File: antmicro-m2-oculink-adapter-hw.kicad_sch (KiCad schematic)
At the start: 10 parts, among them J1 PCB-Edge_M.2_Key-M, J2 OCuLink_x4_Amphenol_G14A42121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

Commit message: [#80280] Fix DRC
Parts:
- added TP3: TP_1.5mm_SMD, antmicro-footprints:TP_SMD_1.5mm, symbol TestPoints:TP_1.5mm_SMD
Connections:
- net at J2.B13 (~{CPRSNT}): now also TP3.1
- no-connect marks 8 -> 7
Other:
- moved on the sheet: R5
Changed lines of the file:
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@@
 		(title " M.2 to OCuLink adapter")
 		(date "2025-07-09")
-		(rev "0")
+		(rev "1.0.0")
 		(company "Antmicro Ltd")
 		(comment 1 "www.antmicro.com")
@@
 	)
 	(no_connect
-		(at 250.19 80.01)
-	)
-	(no_connect
 		(at 55.88 82.55)
 	)
@@
 	(wire
 		(pts
-			(xy 229.87 82.55) (xy 224.79 82.55)
+			(xy 232.41 82.55) (xy 227.33 82.55)
 		)
 		(stroke
@@
 	(wire
 		(pts
-			(xy 250.19 82.55) (xy 234.95 82.55)
+			(xy 250.19 82.55) (xy 237.49 82.55)
 		)
 		(stroke
@@
 	(wire
 		(pts
-			(xy 229.87 77.47) (xy 224.79 77.47)
+			(xy 232.41 77.47) (xy 227.33 77.47)
 		)
 		(stroke
@@
 	(wire
 		(pts
-			(xy 250.19 77.47) (xy 234.95 77.47)
+			(xy 250.19 77.47) (xy 237.49 77.47)
 		)
 		(stroke
@@
 		(pts
 			(xy 40.64 86.36) (xy 40.64 87.63)
+		)
+		(stroke
+			(width 0)
+			(type default)
+		)
+	)
+	(wire
+		(pts
+			(xy 214.63 80.01) (xy 250.19 80.01)
 		)
 		(stroke
@@
 	)
 	(label "~{WAKE}"
-		(at 224.79 82.55 180)
+		(at 227.33 82.55 180)
 		(effects
 			(font
@@
 	)
 	(label "~{PERST}"
-		(at 224.79 77.47 180)
+		(at 227.33 77.47 180)
 		(effects
 			(font
@@
 	)
 	(symbol
+		(lib_id "TestPoints:TP_1.5mm_SMD")
+		(at 214.63 80.01 90)
+		(unit 1)
+		(exclude_from_sim no)
+		(in_bom no)
+		(on_board yes)
+		(dnp no)
+		(property "Reference" "TP3"
+			(at 215.392 76.708 90)
+			(effects
+				(font
+					(size 1.27 1.27)
+					(thickness 0.15)
+				)
+				(justify right)
+			)
+		)
+		(property "Value" "TP_1.5mm_SMD"
+			(at 222.25 64.77 0)
+			(effects
+				(font
+					(size 1.27 1.27)
+					(thickness 0.15)
+				)
+				(justify left bottom)
+				(hide yes)
+			)
+		)
+		(property "Footprint" "antmicro-footprints:TP_SMD_1.5mm"
+			(at 224.79 64.77 0)
+			(effects
+				(font
+					(size 1.27 1.27)
+					(thickness 0.15)
+				)
+				(justify left bottom)
+				(hide yes)
+			)
+		)
+		(property "Datasheet" ""
+			(at 227.33 62.23 0)
+			(effects
+				(font
+					(size 1.27 1.27)
+					(thickness 0.15)
+				)
+				(justify left bottom)
+				(hide yes)
+			)
+		)
+		(property "Description" "test point, SMT"
+			(at 214.63 80.01 0)
+			(effects
+				(font
+					(size 1.27 1.27)
+				)
+				(hide yes)
+			)
+		)
+		(property "MPN" ""
+			(at 214.63 80.01 0)
+			(effects
+				(font
+					(size 1.27 1.27)
+				)
+				(hide yes)
+			)
+		)
+		(property "Manufacturer" ""
+			(at 214.63 80.01 0)
+			(effects
+				(font
+					(size 1.27 1.27)
+				)
+				(hide yes)
+			)
+		)
+		(property "Author" "Antmicro"
+			(at 229.87 64.77 0)
+			(effects
+				(font
+					(size 1.27 1.27)
+					(thickness 0.15)
+				)
+				(justify left bottom)
+				(hide yes)
+			)
+		)
+		(property "License" "Apache-2.0"
+			(at 232.41 64.77 0)
+			(effects
+				(font
+					(size 1.27 1.27)
+					(thickness 0.15)
+				)
+				(justify left bottom)
+				(hide yes)
+			)
+		)
+		(pin "1"
+		)
+		(instances
+			(project "antmicro-m2-oculink-adapter-hw"
+				(path "/b9cca87b-aef2-493b-be4f-d9e02584eafa"
+					(reference "TP3")
+					(unit 1)
+				)
+			)
+		)
+	)
+	(symbol
 		(lib_id "antmicropower:GND")
 		(at 278.13 146.05 0)
@@
 	(symbol
 		(lib_id "antmicroResistors0402:R_0R_0402")
-		(at 234.95 77.47 0)
+		(at 237.49 77.47 0)
 		(mirror y)
 		(unit 1)
@@
 		(dnp no)
 		(property "Reference" "R5"
-			(at 236.728 76.2 0)
+			(at 239.268 76.2 0)
 			(effects
 				(font
@@
 		)
 		(property "Value" "R_0R_0402"
-			(at 214.63 90.17 0)
+			(at 217.17 90.17 0)
 			(effects
 				(font
@@
 		)
 		(property "Footprint" "antmicro-footprints:R_0402_1005Metric"
-			(at 214.63 92.71 0)
+			(at 217.17 92.71 0)
 			(effects
 				(font
@@
 		)
 		(property "Datasheet" "https://industrial.panasonic.com/cdbs/www-data/pdf/RDA0000/AOA0000C301.pdf"
-			(at 214.63 95.25 0)
+			(at 217.17 95.25 0)
 			(effects
 				(font
@@
 		)
 		(property "Description" "SMD Chip Resistor, Jumper, 0 ohm, 100 mW, 0402 [1005 Metric], Thick Film, General Purpose"
-			(at 234.95 77.47 0)
+			(at 237.49 77.47 0)
 			(effects
 				(font
@@
 		)
 		(property "MPN" "ERJ2GE0R00X"
-			(at 214.63 97.79 0)
+			(at 217.17 97.79 0)
 			(effects
 				(font
@@
 		)
 		(property "Manufacturer" "Panasonic"
-			(at 214.63 100.33 0)
+			(at 217.17 100.33 0)
 			(effects
 				(font
@@
 		)
 		(property "License" "Apache-2.0"
-			(at 214.63 102.87 0)
+			(at 217.17 102.87 0)
 			(effects
 				(font
@@
 		)
 		(property "Author" "Antmicro"
-			(at 214.63 105.41 0)
+			(at 217.17 105.41 0)
 			(effects
 				(font
@@
 		)
 		(property "Val" "0R"
-			(at 228.854 76.2 0)
+			(at 231.394 76.2 0)
 			(effects
 				(font
@@
 		)
 		(property "Tolerance" "~"
-			(at 214.63 87.63 0)
+			(at 217.17 87.63 0)
 			(effects
 				(font
@@
 		)
 		(property "Current" "1A"
-			(at 214.63 107.95 0)
+			(at 217.17 107.95 0)
 			(effects
 				(font
@@
 	(symbol
 		(lib_id "antmicroResistors0402:R_0R_0402")
-		(at 234.95 82.55 0)
+		(at 237.49 82.55 0)
 		(mirror y)
 		(unit 1)
@@
 		(dnp no)
 		(property "Reference" "R6"
-			(at 236.728 81.28 0)
-			(effects
-				(font
-					(size 1.27 1.27)
-					(thickness 0.15)
-				)
-				(hide yes)
+			(at 239.268 81.28 0)
+			(effects
+				(font
+					(size 1.27 1.27)
+					(thickness 0.15)
+				)
 			)
 		)
 		(property "Value" "R_0R_0402"
-			(at 214.63 95.25 0)
+			(at 217.17 95.25 0)
 			(effects
 				(font
@@
 		)
 		(property "Footprint" "antmicro-footprints:R_0402_1005Metric"
-			(at 214.63 97.79 0)
+			(at 217.17 97.79 0)
 			(effects
 				(font
@@
 		)
 		(property "Datasheet" "https://industrial.panasonic.com/cdbs/www-data/pdf/RDA0000/AOA0000C301.pdf"
-			(at 214.63 100.33 0)
+			(at 217.17 100.33 0)
 			(effects
 				(font
@@
 		)
 		(property "Description" "SMD Chip Resistor, Jumper, 0 ohm, 100 mW, 0402 [1005 Metric], Thick Film, General Purpose"
-			(at 234.95 82.55 0)
+			(at 237.49 82.55 0)
 			(effects
 				(font
@@
 		)
 		(property "MPN" "ERJ2GE0R00X"
-			(at 214.63 102.87 0)
+			(at 217.17 102.87 0)
 			(effects
 				(font
@@
 		)
 		(property "Manufacturer" "Panasonic"
-			(at 214.63 105.41 0)
+			(at 217.17 105.41 0)
 			(effects
 				(font
@@
 		)
 		(property "License" "Apache-2.0"
-			(at 214.63 107.95 0)
+			(at 217.17 107.95 0)
 			(effects
 				(font
@@
 		)
 		(property "Author" "Antmicro"
-			(at 214.63 110.49 0)
+			(at 217.17 110.49 0)
 			(effects
 				(font
@@
 		)
 		(property "Val" "0R"
-			(at 228.854 81.28 0)
+			(at 231.394 81.28 0)
 			(effects
 				(font
@@
 		)
 		(property "Tolerance" "~"
-			(at 214.63 92.71 0)
+			(at 217.17 92.71 0)
 			(effects
 				(font
@@
 		)
 		(property "Current" "1A"
-			(at 214.63 113.03 0)
-			(effects
-				(font
+			(at 217.17 113.03 0)
+			(effects
+				(font

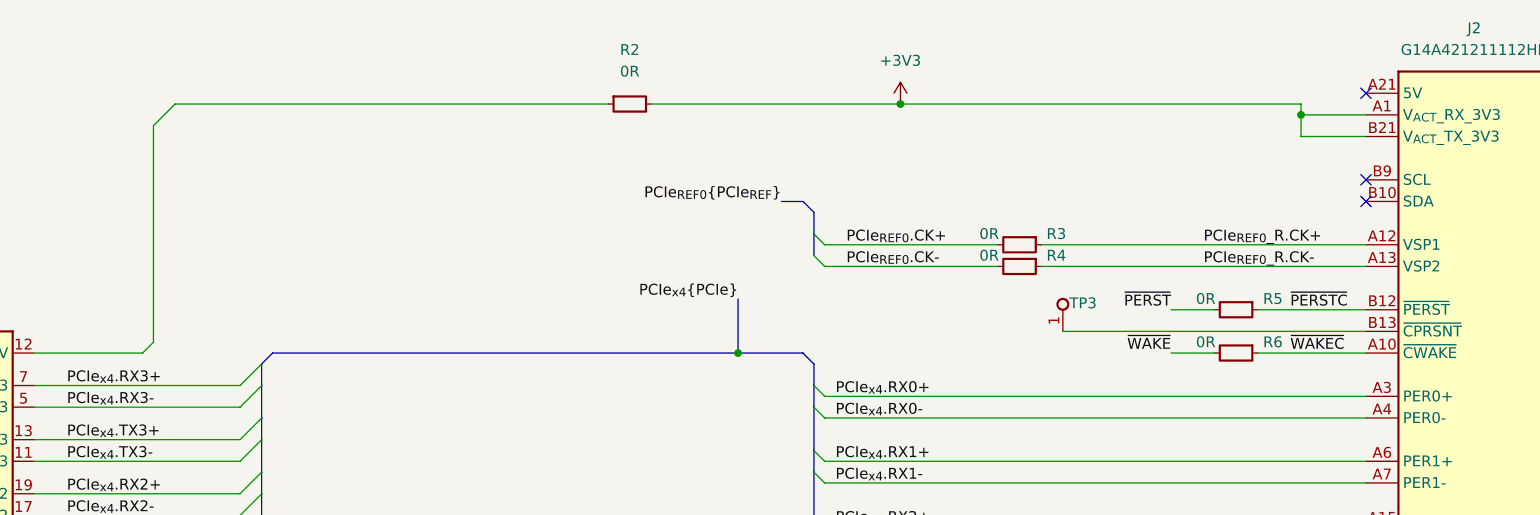
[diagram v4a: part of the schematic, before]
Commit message: [#81131] Change resistor, testpoint sizing. Add 0R to 3V3 and ~CWAKE
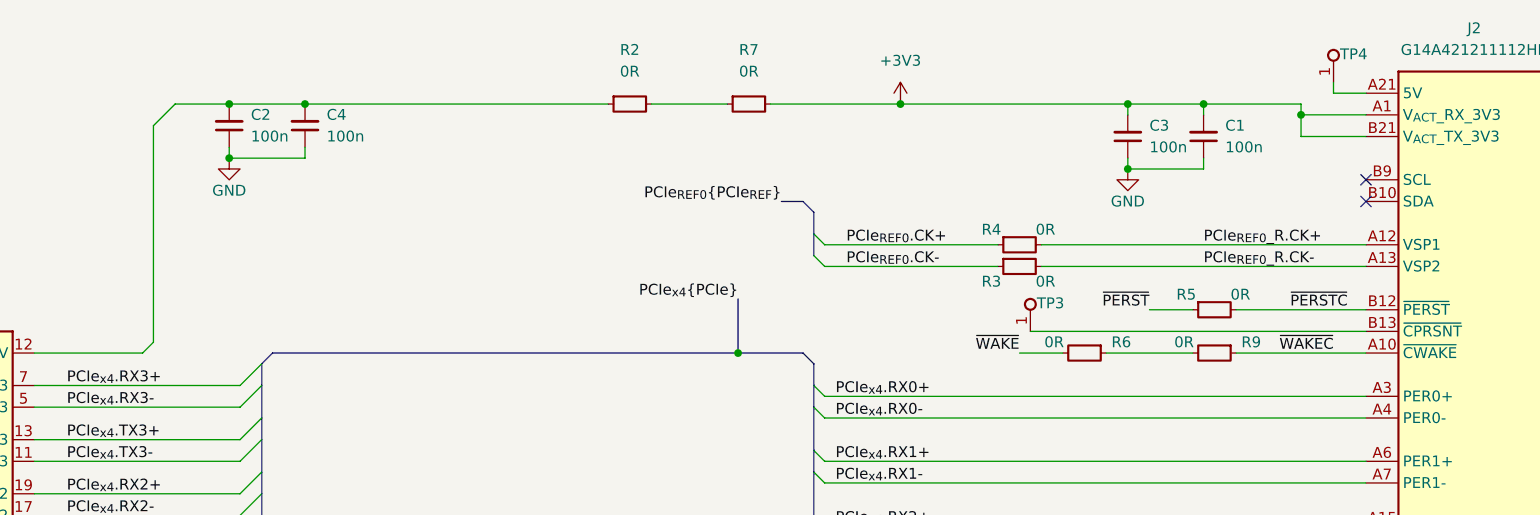
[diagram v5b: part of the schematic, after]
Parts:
- removed R3, R4, R5: R_0R_0402, antmicro-footprints:R_0402_1005Metric, symbol antmicroResistors0402:R_0R_0402
- added C1, C2, C3, C4: C_100n_16V_X7R_0402, antmicro-footprints:C_0402_1005Metric, symbol Capacitors0402:C_100n_16V_X7R_0402
- added R3, R4, R5: R_0R_0201, antmicro-footprints:R_0201, symbol antmicroResistorsmisc:R_0R_0201
- added R7: R_0R_0402, antmicro-footprints:R_0402_1005Metric, symbol Resistors0402:R_0R_0402
- added R9: R_0R_0402, antmicro-footprints:R_0402_1005Metric, symbol antmicroResistors0402:R_0R_0402
- added TP4: TP_1.5mm_SMD, antmicro-footprints:TP_SMD_1.5mm, symbol TestPoints:TP_1.5mm_SMD
- TP3: footprint antmicro-footprints:TP_SMD_1.5mm -> antmicro-footprints:TP_SMD_0.75mm
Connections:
- net +3V3: now also C1.2, C3.2, R7.2; no longer R2.2
- net GND: now also C1.1, C2.1, C3.1, C4.1
- net PCIe_{REF0}.CK+: now also R4.1
- net PCIe_{REF0}.CK-: now also R3.1
- net PCIe_{REF0}_R.CK+: now also R4.2
- net PCIe_{REF0}_R.CK-: now also R3.2
- net ~{PERSTC}: now also R5.2
- net ~{PERST}: now also R5.1
- net ~{WAKEC}: now also R9.1; no longer R6.1
- net at J1.12 (3.3V), J1.14 (3.3V), J1.16 (3.3V)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: now also C2.2, C4.2
- net at J2.A21 (5V), J2.B1 (5V): now also TP4.1
- new net: R2.2, R7.1
- new net: R6.1, R9.2
- no-connect marks 7 -> 6
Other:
- moved on the sheet: R6, TP3

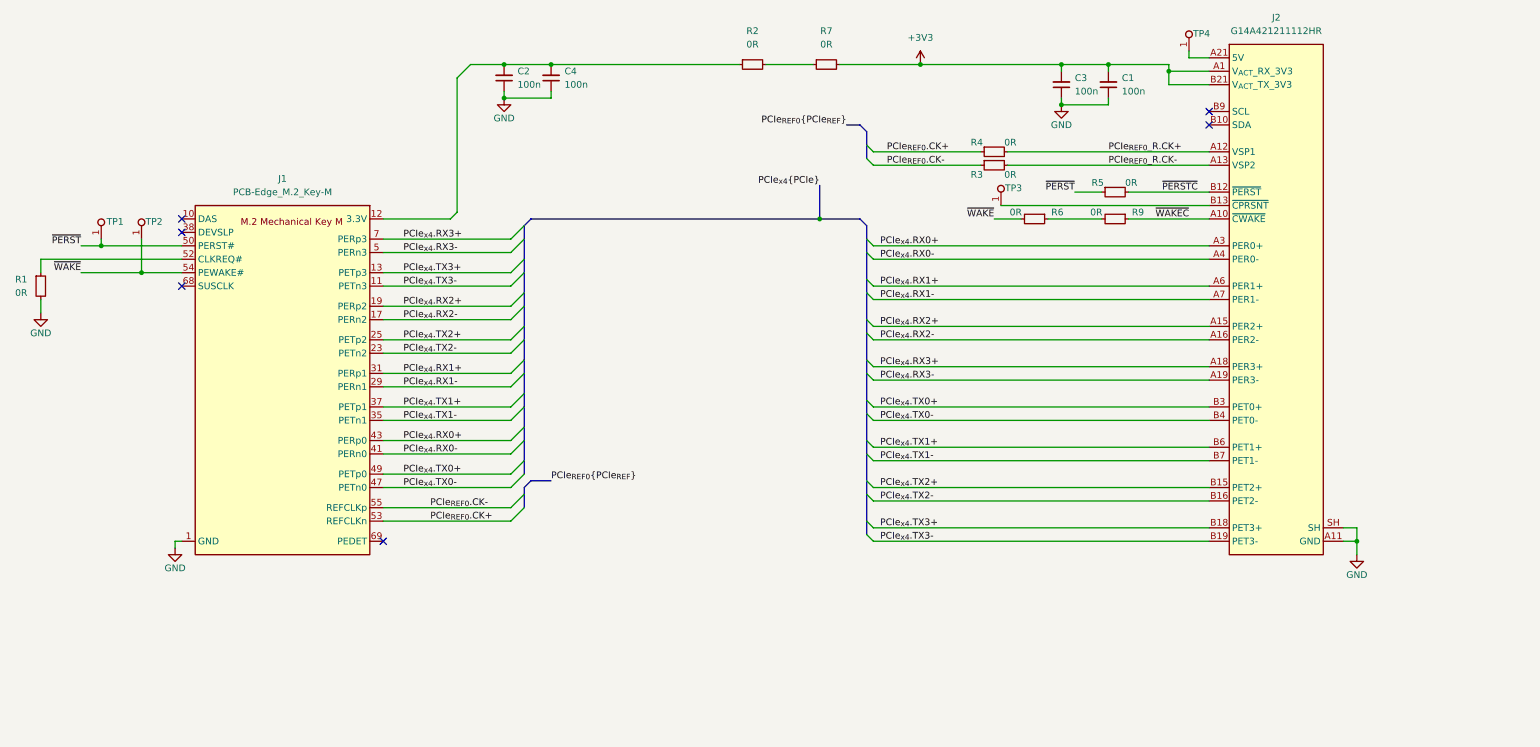
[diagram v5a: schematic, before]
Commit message: [#81131] Add 0R selector for refclk
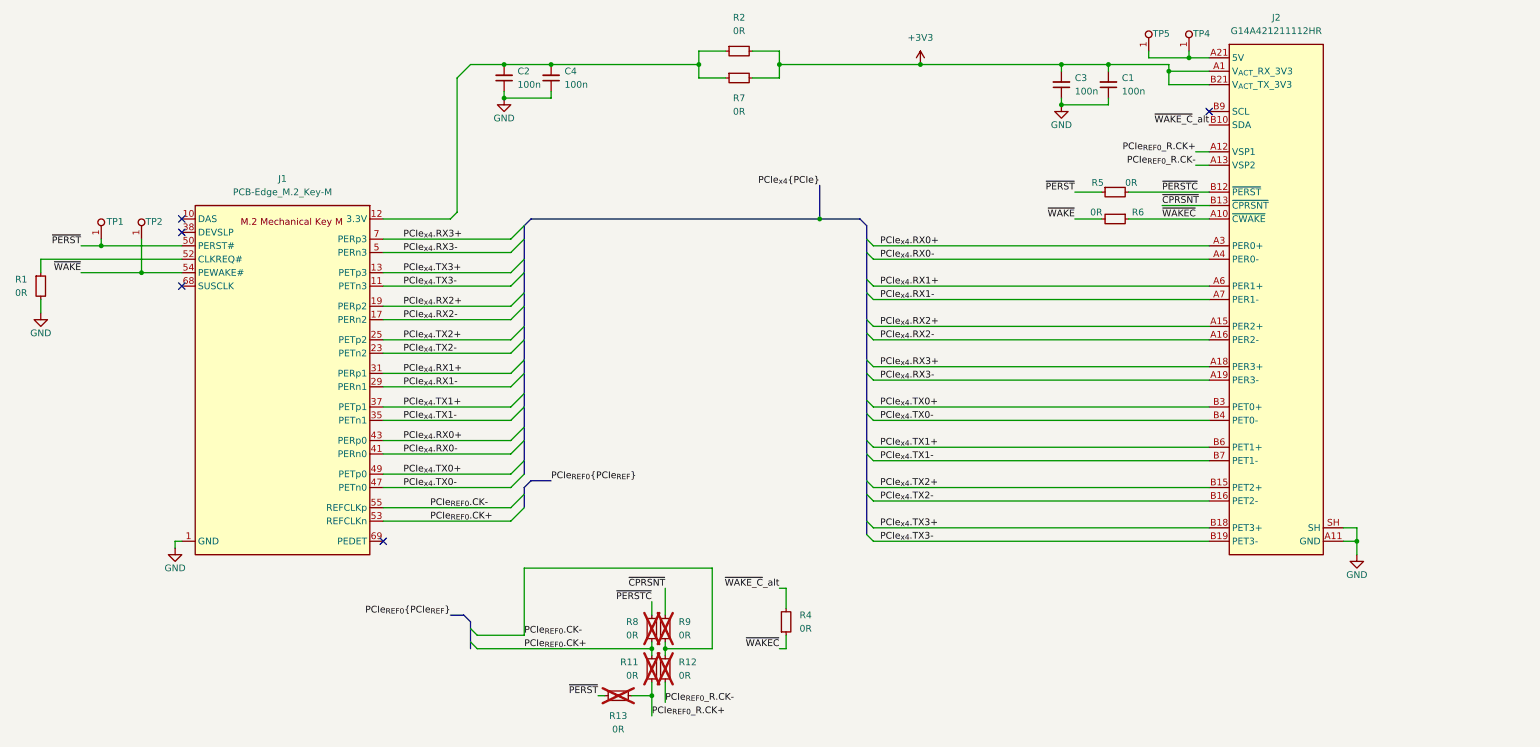
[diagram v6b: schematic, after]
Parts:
- removed R3: R_0R_0201, antmicro-footprints:R_0201, symbol antmicroResistorsmisc:R_0R_0201
- removed R9: R_0R_0402, antmicro-footprints:R_0402_1005Metric, symbol antmicroResistors0402:R_0R_0402
- removed TP3: TP_1.5mm_SMD, antmicro-footprints:TP_SMD_0.75mm, symbol TestPoints:TP_1.5mm_SMD
- added R11, R12, R13, R8, R9: R_0R_0201, antmicro-footprints:R_0201, symbol antmicroResistorsmisc:R_0R_0201
- added TP5: TP_1.5mm_SMD, antmicro-footprints:TP_SMD_1.5mm, symbol TestPoints:TP_1.5mm_SMD
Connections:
- net +3V3: now also R2.2
- net PCIe_{REF0}.CK+: now also R11.2, R8.1; no longer R4.1
- net PCIe_{REF0}.CK-: now also R12.2, R9.1
- net PCIe_{REF0}_R.CK+: now also R11.1, R13.1; no longer R4.2
- net PCIe_{REF0}_R.CK-: now also R12.1
- net ~{PERSTC}: now also R8.2
- net ~{PERST}: now also R13.2
- net ~{WAKEC}: now also R4.1, R6.1
- net at C2.2, C4.2, J1.12 (3.3V)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: now also R7.1
- net at J2.A21 (5V), J2.B1 (5V), TP4.1: now also TP5.1
- net ~{CPRSNT}: now reaches J2.B13 (~{CPRSNT})
- net ~{CPRSNT}: now also R9.2
- net ~{WAKE_C}_alt: now reaches J2.B10 (SDA)
- net ~{WAKE_C}_alt: now also R4.2
- no-connect marks 6 -> 5
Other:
- moved on the sheet: R2, R6, R7
